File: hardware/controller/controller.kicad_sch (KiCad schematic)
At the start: 0 parts

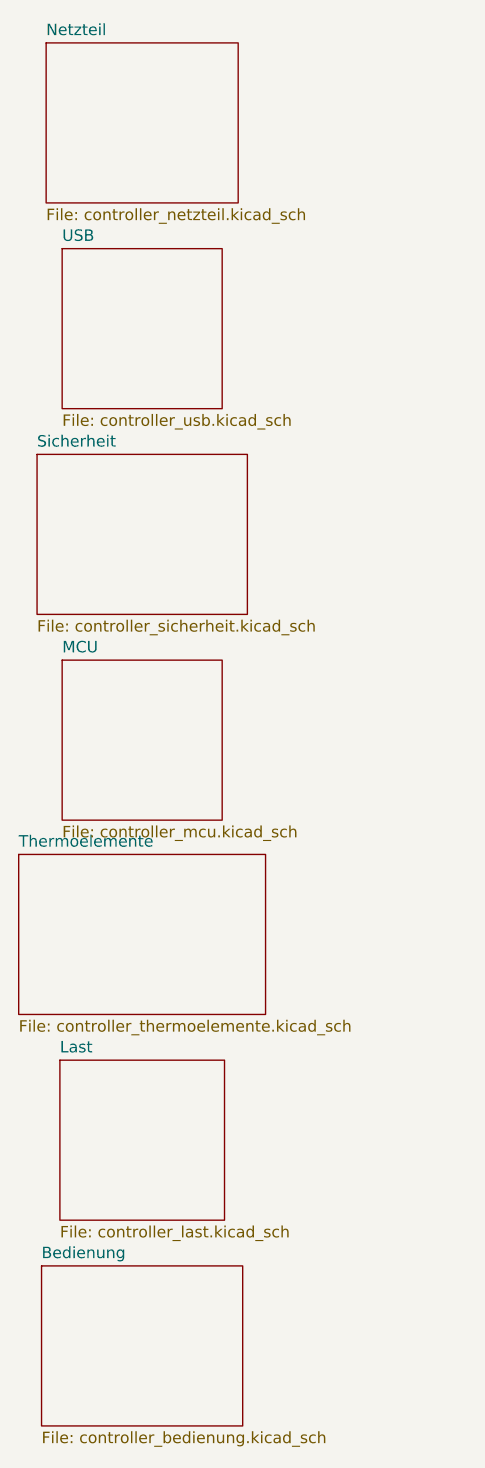
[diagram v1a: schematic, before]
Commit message: refactor(hardware): merge the 7 controller sheets into 2 (T071)
"Leistung und Sicherheit" (A3: Netzteil, Sicherheit, Last) and
"Steuerung und Messung" (A2: MCU, USB, Thermoelemente, Bedienung).
Contents are only moved, not rewired; each former sheet gets a labelled
frame. check_schematic: 119 parts, 69 nets, 0 errors; ERC unchanged.
PCB relinked by reference, placement unchanged, parity DRC clean.

Co-Authored-By: Claude Opus 5.5 <noreply@anthropic.com>
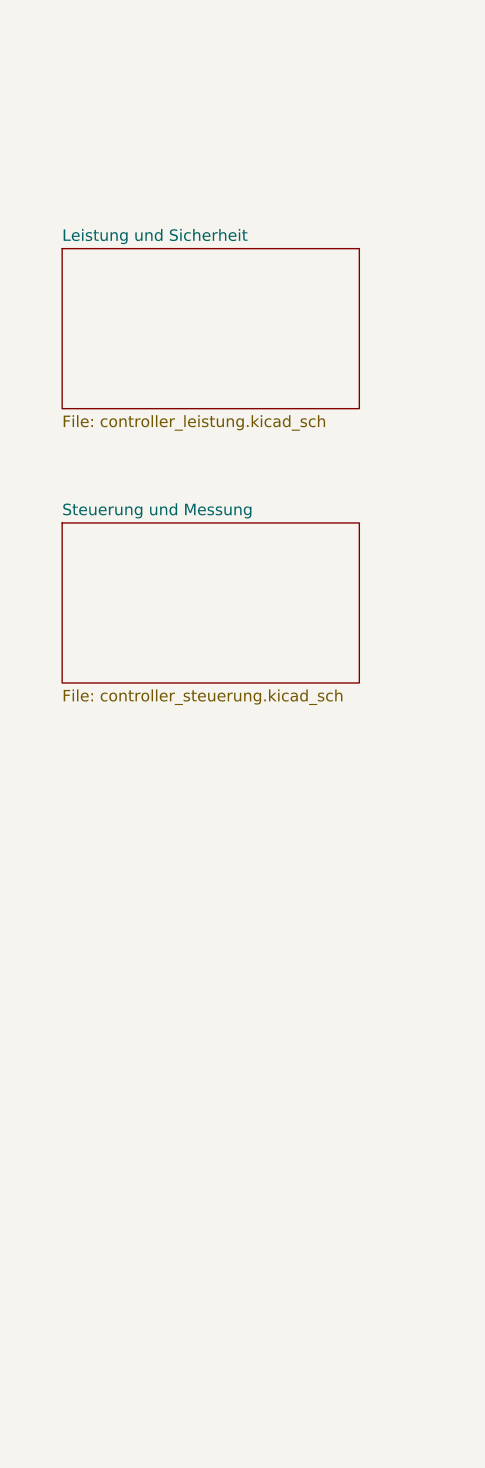
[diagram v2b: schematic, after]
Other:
- sheet MCU renamed Steuerung und Messung
- sheet Netzteil renamed Leistung und Sicherheit
- removed sheet Bedienung
- removed sheet Last
- removed sheet Sicherheit
- removed sheet Thermoelemente
- removed sheet USB
- sheet Leistung und Sicherheit: file controller_netzteil.kicad_sch -> controller_leistung.kicad_sch
- sheet Steuerung und Messung: file controller_mcu.kicad_sch -> controller_steuerung.kicad_sch
